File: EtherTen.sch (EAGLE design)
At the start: 103 parts, among them IC1 MC33269DT-5.0, IC2 APX811-44UG-7, IC3 ATMEGA16U2-MU, IC4 LM358D, IC5 ATMEGA328P TQFP32, IC6 W5100SQFP80, IC7 MCP24AA025E48, J1 DC_2_1MM, P1 USB-6PSMT, P2 ICSP:MAIN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

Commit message: Replaced most parts using SuperHouse library to add 3D models
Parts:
- C1, C11, C12, C14, C15, C16, C17, C18, C19, C2, C20, C21, C22, C23, C24, C25, C26, C27, C28, C29, C7, C8, C9: device freetronics:CAP0603 -> SuperHouse-DiscreteSemi:CAP0603
- C10, C13, C3, C4: device freetronics:CAP_POL1206 -> SuperHouse-DiscreteSemi:CAP_POL1206
- D1: device freetronics:DIODESMB -> SuperHouse-DiscreteSemi:DIODESMA
- F1: device rcl:L-EUL1812 -> SuperHouse-Fuses:PTC050
- H1: device freetronics-original:M100.1 -> SuperHouse-Connectors:M10-SOCKET
- H2: device freetronics-master-v1:M08 -> SuperHouse-Connectors:M08-SOCKET
- H3: device freetronics:M06SIP -> SuperHouse-Connectors:M06-SOCKET
- H4: device freetronics:M08 -> SuperHouse-Connectors:M08-SOCKET
- IC2: device freetronics-master-v1:APX81X-RESET-IC -> SuperHouse-ICs:APX81X
- IC3: device freetronics-jon:ATMEL_ATMEGA8U2-MUQFN -> SuperHouse-MCUs:ATMEGA8U2QFN
- IC4: device linear:LM358D -> SuperHouse-ICs:LM358D
- IC5: device freetronics-2:AVR-MEGA8-AI -> SuperHouse-MCUs:AVR-MEGA8-AI
- IC6: device freetronics-marc:W5100SQFP80 -> SuperHouse-ICs:W5100SQFP80
- J1: device freetronics:POWER_JACKPTH -> SuperHouse-Connectors:POWER_JACK-SLOTS
- L3: device freetronics-master-v1:INDUCTOR0805-LARGE -> SuperHouse-DiscreteSemi:INDUCTOR0805-LARGE
- LED1, LED10, LED2, LED3, LED4, LED5, LED6, LED7, LED8, LED9: device freetronics:LED0603 -> SuperHouse-LEDs:LED0603
- P1: value USB-6PSMT -> USB-6P-SMT; device freetronics-jon:USB-6PSMT -> SuperHouse-Connectors:USB-6P-SMT
- P2, P3: device pinhead:PINHD-2X3 -> SuperHouse-Connectors:ICSPPTH
- P4: device freetronics-master-v1:USD-SOCKETNEW -> SuperHouse-Connectors:USD-SOCKETNEW
- Q3: device freetronics:MOSFET-NCHANNELSMD -> SuperHouse-DiscreteSemi:MOSFET-NCHANNEL-233
- R1, R2, R3, R4, R5, R6, R7, R8: device freetronics:RESISTOR0603 -> SuperHouse-DiscreteSemi:RESISTOR0603
- R14, R15: device freetronics-master-v1.1:RESISTOR0603 -> SuperHouse-DiscreteSemi:RESISTOR0603
- RN1, RN2, RN3, RN4, RN5, RN6, RN7, RN8: device freetronics-master-v1:4R-NCAY16 -> SuperHouse-DiscreteSemi:4R-NCAY16
- S1: device freetronics:TAC_SWITCHSMD -> SuperHouse-Switches:TAC_SWITCH-SMT-6
- U1: device freetronics-jon:HY931147C-RJ45 -> SuperHouse-Connectors:HY931147C-RJ45
- X1, X2, X3: device freetronics-master-v1:CRYSTALHC49UV -> SuperHouse-Oscillators:CRYSTALHC49UV
- Z1, Z2: device freetronics:RESISTOR0603 -> SuperHouse-DiscreteSemi:TVS0603

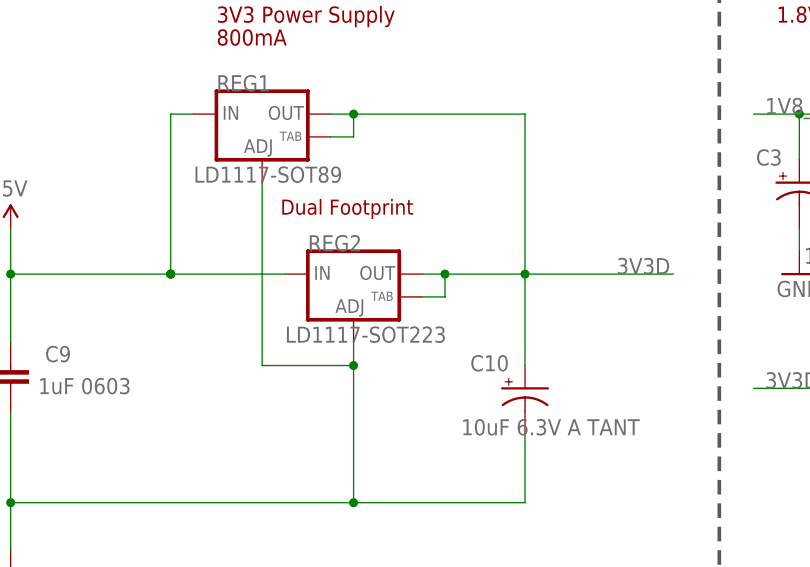
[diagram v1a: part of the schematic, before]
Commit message: Replaced more parts using SuperHouse libraries
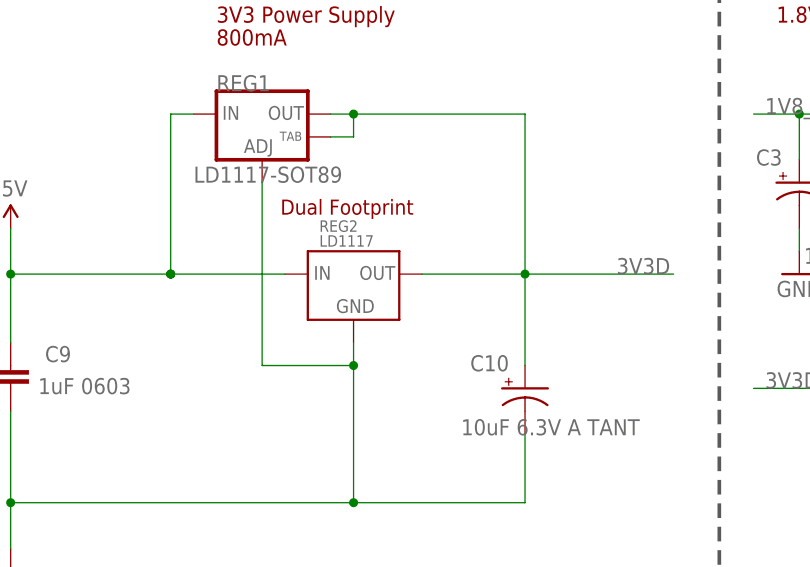
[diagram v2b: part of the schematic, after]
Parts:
- Q2: device freetronics:MOSFET-NCHANNELSMD -> SuperHouse-DiscreteSemi:MOSFET-NCHANNEL-233
- REG2: value LD1117-SOT223 -> LD1117; device freetronics:V_REG_LM1117SOT223 -> SuperHouse-Regulators:LD1117
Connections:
- net 3V3D: no longer REG2.OUT@1
- net GND: now also REG2.GND; no longer REG2.ADJ
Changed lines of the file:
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@@
 <part name="FID1" library="freetronics" deviceset="FIDUCIAL" device="1X2.5"/>
 <part name="FID2" library="freetronics" deviceset="FIDUCIAL" device="1X2.5"/>
-<part name="REG2" library="freetronics" deviceset="V_REG_LM1117" device="SOT223" value="LD1117-SOT223"/>
 <part name="REG1" library="freetronics" deviceset="V_REG_LM1117" device="SOT89" value="LD1117-SOT89"/>
 <part name="U1" library="SuperHouse-Connectors" library_urn="urn:adsk.eagle:library:11765989" deviceset="HY931147C" device="-RJ45" package3d_urn="urn:adsk.eagle:package:11872177/2"/>
@@
 <part name="U$1" library="SparkFun" deviceset="5V" device=""/>
 <part name="U$4" library="SparkFun" deviceset="5V" device=""/>
-<part name="Q2" library="freetronics" deviceset="MOSFET-NCHANNEL" device="SMD" value="2N7002"/>
+<part name="Q2" library="SuperHouse-DiscreteSemi" library_urn="urn:adsk.eagle:library:11768461" deviceset="MOSFET-NCHANNEL" device="-233" package3d_urn="urn:adsk.eagle:package:11815952/3" value="2N7002"/>
 <part name="GND33" library="SparkFun" deviceset="GND" device=""/>
 <part name="LED10" library="SuperHouse-LEDs" library_urn="urn:adsk.eagle:library:11790571" deviceset="LED" device="0603" package3d_urn="urn:adsk.eagle:package:7066240/3" value="D13/RED"/>
@@
 <part name="SJ6" library="freetronics-jon" library_urn="urn:adsk.eagle:library:7065448" deviceset="SJC" device="N" package3d_urn="urn:adsk.eagle:package:7066342/1" value="SJCN"/>
 <part name="U$6" library="SparkFun" deviceset="5V" device=""/>
+<part name="REG2" library="SuperHouse-Regulators" library_urn="urn:adsk.eagle:library:11786698" deviceset="LD1117" device="" package3d_urn="urn:adsk.eagle:package:11860990/2"/>
 </parts>
 <sheets>
@@
 <instance part="FID1" gate="G$1" x="241.3" y="15.24" smashed="yes"/>
 <instance part="FID2" gate="G$1" x="241.3" y="10.16" smashed="yes"/>
-<instance part="REG2" gate="G$1" x="48.26" y="149.86" smashed="yes">
-<attribute name="NAME" x="43.18" y="152.4" size="1.778" layer="95"/>
-<attribute name="VALUE" x="40.64" y="142.24" size="1.778" layer="96"/>
-</instance>
 <instance part="REG1" gate="G$1" x="38.1" y="167.64" smashed="yes">
 <attribute name="NAME" x="33.02" y="170.18" size="1.778" layer="95"/>
@@
 <instance part="U$6" gate="G$1" x="396.24" y="88.9" smashed="yes">
 <attribute name="VALUE" x="395.224" y="92.456" size="1.778" layer="96"/>
+</instance>
+<instance part="REG2" gate="G$1" x="48.26" y="147.32" smashed="yes">
+<attribute name="NAME" x="44.45" y="154.559" size="1.27" layer="95"/>
+<attribute name="VALUE" x="44.45" y="152.908" size="1.27" layer="96"/>
 </instance>
 </instances>
@@
 <junction x="48.26" y="139.7"/>
 <pinref part="GND13" gate="1" pin="GND"/>
-<pinref part="REG2" gate="G$1" pin="ADJ"/>
 <pinref part="C10" gate="G$1" pin="-"/>
 <pinref part="C9" gate="G$1" pin="2"/>
 <pinref part="REG1" gate="G$1" pin="ADJ"/>
+<pinref part="REG2" gate="G$1" pin="GND"/>
 </segment>
 <segment>
@@
 <wire x1="67.31" y1="139.7" x2="67.31" y2="149.86" width="0.1524" layer="91"/>
 <wire x1="67.31" y1="167.64" x2="67.31" y2="149.86" width="0.1524" layer="91"/>
-<wire x1="55.88" y1="149.86" x2="58.42" y2="149.86" width="0.1524" layer="91"/>
-<wire x1="58.42" y1="149.86" x2="67.31" y2="149.86" width="0.1524" layer="91"/>
-<wire x1="55.88" y1="147.32" x2="58.42" y2="147.32" width="0.1524" layer="91"/>
-<wire x1="58.42" y1="147.32" x2="58.42" y2="149.86" width="0.1524" layer="91"/>
+<wire x1="55.88" y1="149.86" x2="67.31" y2="149.86" width="0.1524" layer="91"/>
 <wire x1="45.72" y1="167.64" x2="48.26" y2="167.64" width="0.1524" layer="91"/>
 <wire x1="48.26" y1="167.64" x2="67.31" y2="167.64" width="0.1524" layer="91"/>
@@
 <wire x1="48.26" y1="165.1" x2="48.26" y2="167.64" width="0.1524" layer="91"/>
 <junction x="67.31" y="149.86"/>
-<junction x="58.42" y="149.86"/>
 <junction x="48.26" y="167.64"/>
 <label x="77.47" y="149.86" size="1.778" layer="95"/>
-<pinref part="REG2" gate="G$1" pin="OUT"/>
-<pinref part="REG2" gate="G$1" pin="OUT@1"/>
 <pinref part="REG1" gate="G$1" pin="OUT"/>
 <pinref part="REG1" gate="G$1" pin="OUT@1"/>
 <pinref part="C10" gate="G$1" pin="+"/>
+<pinref part="REG2" gate="G$1" pin="OUT"/>
 </segment>
 <segment>
@@
 <junction x="10.16" y="149.86"/>
 <junction x="27.94" y="149.86"/>
-<pinref part="REG2" gate="G$1" pin="IN"/>
 <pinref part="REG1" gate="G$1" pin="IN"/>
 <pinref part="U$5" gate="G$1" pin="5V"/>
 <pinref part="C9" gate="G$1" pin="1"/>
-</segment>
-<segment>
+<pinref part="REG2" gate="G$1" pin="IN"/>
+</segment>
+<segment>
